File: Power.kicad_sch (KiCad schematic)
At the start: 42 parts, among them J1 XT60_BAT, J102 E_STOP, Q1 SQJ459EP-T1_GE3, U1 LMR36520FADDA, U2 AP2112K-3.3

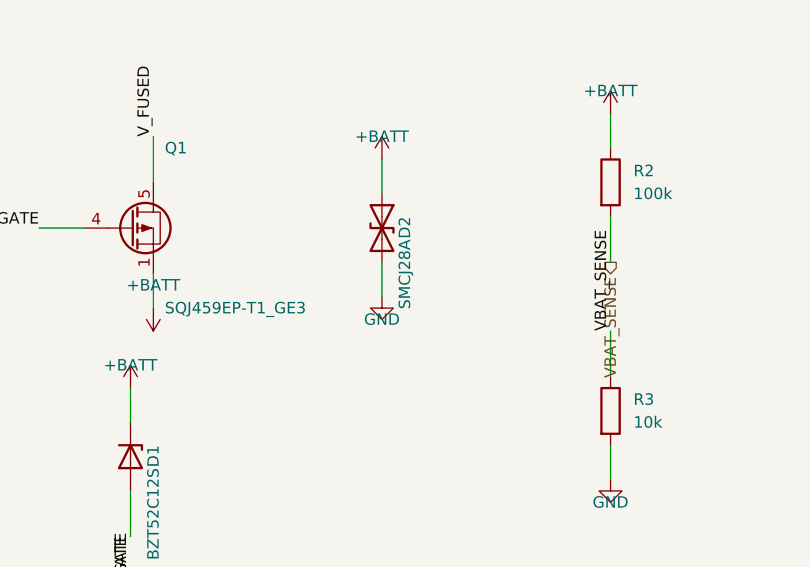
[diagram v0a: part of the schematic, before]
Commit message: Resolve all 5 prototype review items (F1 3557-2 4-pad THT, SMCJ30A, 2.2nF/0.5W snubber, 0.45-0.50mm stepper traces, clean PTH/NPTH drills)
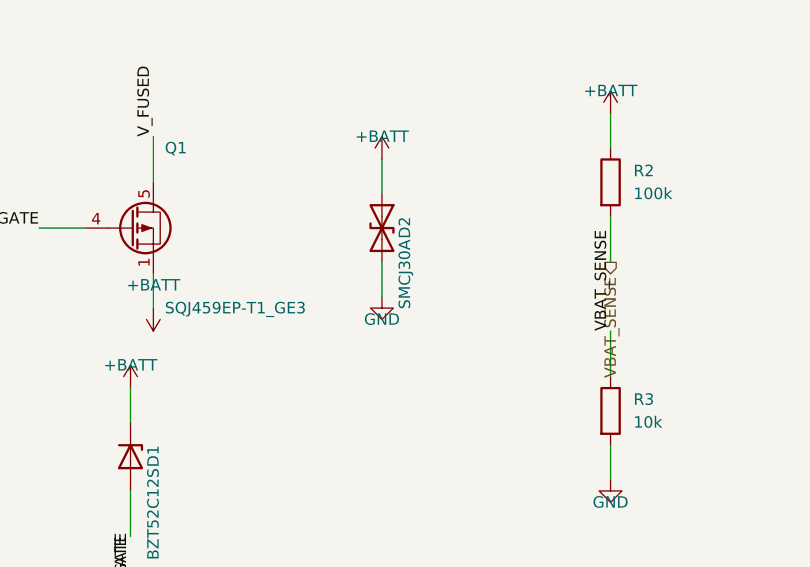
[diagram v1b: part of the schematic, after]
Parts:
- D2: value SMCJ28A -> SMCJ30A
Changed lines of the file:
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@@
 			)
 		)
-		(property "Value" "SMCJ28A"
+		(property "Value" "SMCJ30A"
 			(at 144.78 72.39 0)
 			(effects

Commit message: Release v1.0-production: finalize F1 3D STEP model alignment and archive V1.0 production package
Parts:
- F1: footprint Fuse:Fuse_Blade_ATO_directSolder -> abx-footprints:Fuseholder_Keystone_3557-2
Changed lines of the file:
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@@
 			)
 		)
-		(property "Footprint" "Fuse:Fuse_Blade_ATO_directSolder"
+		(property "Footprint" "abx-footprints:Fuseholder_Keystone_3557-2"
 			(at 71.12 71.12 0)
 			(effects

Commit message: brushless
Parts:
- removed C5: 1uF, Capacitor_SMD:C_0603_1608Metric, symbol Device:C
- removed U1: LMR36520FADDA, Package_SO:Texas_HSOP-8-1EP_3.9x4.9mm_P1.27mm_ThermalVias, symbol Regulator_Switching:LMR33630ADDA
- added C11, C904: 10nF, Capacitor_SMD:C_0603_1608Metric, symbol Device:C
- added C12, C911: 68pF C0G, Capacitor_SMD:C_0603_1608Metric, symbol Device:C
- added C901, C902: 4.7uF/100V, Capacitor_SMD:C_1206_3216Metric, symbol Device:C
- added C903: 100nF/100V, Capacitor_SMD:C_0603_1608Metric, symbol Device:C
- added C905: 100nF, Capacitor_SMD:C_0603_1608Metric, symbol Device:C
- added C906, C907: 47uF/10V, Capacitor_SMD:C_1206_3216Metric, symbol Device:C
- added C908, C909: 1uF, Capacitor_SMD:C_0603_1608Metric, symbol Device:C
- added C910: 10uF, Capacitor_SMD:C_0805_2012Metric, symbol Device:C
- added D3, D902: PDS5100-13, Diode_SMD:D_PowerDI-5, symbol Device:D_Schottky
- added D901: SMAJ5.0A, Diode_SMD:D_SMA, symbol Device:D_TVS
- added J511: 5V_AUX, TerminalBlock_Phoenix:TerminalBlock_Phoenix_MKDS-1,5-2-5.08_1x02_P5.08mm_Horizontal, symbol Connector:Conn_01x02_Pin
- added L901: 10uH MWSA0603S-100MT, Inductor_SMD:L_Sunlord_MWSA0603S, symbol Device:L
- added R10, R903: 196k, Resistor_SMD:R_0603_1608Metric, symbol Device:R
- added R11, R904: 9.1k, Resistor_SMD:R_0603_1608Metric, symbol Device:R
- added R12, R907: 560k, Resistor_SMD:R_0805_2012Metric, symbol Device:R
- added R13, R908: 33k, Resistor_SMD:R_0603_1608Metric, symbol Device:R
- added R901: 53.6k, Resistor_SMD:R_0603_1608Metric, symbol Device:R
- added R902: 10.2k, Resistor_SMD:R_0603_1608Metric, symbol Device:R
- added R905: 39k, Resistor_SMD:R_0603_1608Metric, symbol Device:R
- added R906: 10k, Resistor_SMD:R_0603_1608Metric, symbol Device:R
- added U1, U901: TPS54360BDDAR, Package_SO:TI_SO-PowerPAD-8_ThermalVias, symbol Regulator_Switching:TPS54360DDA
- added U902: TPS25200DRVR, Package_SON:WSON-6-1EP_2x2mm_P0.65mm_EP1x1.6mm_ThermalVias, symbol abx:TPS25200DRV
- C2, C3: value 4.7uF -> 4.7uF/100V
- C4: value 100nF -> 100nF/100V
- C7, C8: value 22uF -> 47uF/10V
- D2: value SMCJ30A -> SMCJ43A
- F1: value 25A -> 10A 58V ATO
- J1: value XT60_BAT -> BATTERY_IN DG135T-10.16-02P; footprint Connector_AMASS:AMASS_XT60-M_1x02_P7.20mm_Vertical -> abx-footprints:ABX_Degson_DG135T-10.16-02P
- L1: value 15uH -> 10uH MWSA0603S-100MT; footprint Inductor_SMD:L_Bourns_SRP7028A_7.3x6.6mm -> Inductor_SMD:L_Sunlord_MWSA0603S
- R3: value 10k -> 6.8k
- R4: value 100k -> 53.6k
- R5: value 24.9k -> 10.2k
- R6: value 10k -> 22k
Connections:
- net +3V3: now also R906.1
- net +BATT: now also C901.1, C902.1, C903.1, R12.1, R907.1, U1.2 (VIN), U901.2 (VIN)
- net GND: now also C11.2, C12.2, C901.2, C902.2, C903.2, C904.2, C906.2, C907.2, C908.2, C909.2, C910.2, C911.2, D3.2 (A), D901.2 (A2), D902.2 (A), J511.2 (Pin_2), R10.2, R13.2, R902.2, R903.2, R905.2, R908.2, U1.7 (GND), U1.9 (GNDPAD), U901.7 (GND), U901.9 (GNDPAD), U902.5 (GND), U902.7 (PAD)
- net U1_BOOT: now also U1.1 (BOOT)
- net U1_FB: now also U1.5 (FB)
- net U1_SW: now also D3.1 (K), U1.8 (SW)
- net V_RAW_IN renamed VBAT_IN
- new net +5V_AUX: C910.1, D901.1 (A1), J511.1 (Pin_1), U902.1 (OUT)
- new net 5V_AUX_BUCK: C906.1, C907.1, C908.1, C909.1, L901.2, R901.1, U902.4 (EN), U902.6 (IN)
- new net AUX5_FLT_N: R906.2, U902.3 (FAULT)
- new net U1_COMP: C12.1, R11.1, U1.6 (COMP)
- new net U1_CZ: C11.1, R11.2
- new net U1_EN: R12.2, R13.1, U1.3 (EN)
- new net U1_RT: R10.1, U1.4 (RT/CLK)
- new net U901_BOOT: C905.1, U901.1 (BOOT)
- new net U901_COMP: C911.1, R904.1, U901.6 (COMP)
- new net U901_CZ: C904.1, R904.2
- new net U901_EN: R907.2, R908.1, U901.3 (EN)
- new net U901_FB: R901.2, R902.1, U901.5 (FB)
- new net U901_RT: R903.1, U901.4 (RT/CLK)
- new net U901_SW: C905.2, D902.1 (K), L901.1, U901.8 (SW)
- new net U902_ILIM: R905.1, U902.2 (ILIM)
- no-connect marks 2 -> 1
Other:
- note added: "+5V/+3V3 are up before the 30.7 V bus-breaker UVLO and stay up below its 26.8 V UV gate."
- note added: "+5V_AUX EXTERNAL OUTPUT (2 A): own buck U901 = same TPS54360B design as U1 (5.00 V, 494 kHz, 10 uH), fed from +BATT (before the bus breaker)"
- note added: "BATTERY INPUT (J1): two solder pads for 8 AWG leads, pin 1 = BAT+ (VBUS, motor bus), pin 2 = BAT-. Sized for 60 A peak (2 x 30 A). Main fuse 80 A (ANL/MIDI) and an anti-spark pre-charge/contactor go in the battery lead OUTSIDE this board. F1 protects the logic branch (5 V buck + LDO, +24V aux buck), 10 A 58 V blade."
- note added: "BOARD +5V BUCK U1 = TPS54360B (replaces LMR36520, 2026-10-24)"
- note added: "EN/UVLO R12 560k / R13 33k: start 20.9 V / stop 19.0 V typ (tolerance 18.8-23.0 V / 16.2-21.8 V):"
- note added: "L1 10 uH, D3 PDS5100-13, comp R11 9.1k + C11 10 nF // C12 68 pF; Cin C2/C3 + C4, BOOT C6, Cout C7/C8 47 uF/10 V."
- note added: "Loads: AP2112 U2/U705, J304/J404/J703, CAN U704, LM339 U802, LEDs: < 1.5 A worst case (IC 3.5 A)."
- note added: "Same design as U901 below: 494 kHz (R10 196k), 5.00 V = 0.8 V x (1 + R4 53.6k / R5 10.2k)."
- note added: "U1 TPS54360B: see the block at the right (x 375-500)."
- note added: "U901 is rated 3.5 A (4.5 A min switch limit): 2 A continuous has margin. IC ~0.55 W, D902 ~1.3 W at 42 V in / 2 A out (give D902 copper)."
- note added: "U902 TPS25200 eFuse (EN tied on): RILIM R905 39k -> 2.33 A min / 2.49 A typ / 2.65 A max (SLVSCJ0F eq. 1), 2.6 A continuous rating, 5.4 V OUT clamp. FAULT -> AUX5_FLT_N (R906 10k to +3V3) -> STM32 PD11. D901 SMAJ5.0A clamps outside transients at J511."
